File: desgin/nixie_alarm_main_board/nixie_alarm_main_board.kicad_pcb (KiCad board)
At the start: 2 copper layers, 79 parts, among them IC1 LM3488MM, IC2 HV5530PG-G, IC4 HV5530PG-G, IC5 TPH5200FNH, IC6 CD40109BQNSRQ1, IC7 AP7363-33D-13, IC8 MCP4018T-502E_LT, J1 DCPLUG 2x6.4mm 2A, J2 JST XH 2.54 3 pin, J3 USB_C_Receptacle_USB2.0_16P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

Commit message: filter caps
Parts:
- removed BZ1: Buzzer, Buzzer_Beeper:MagneticBuzzer_PUI_AT-0927-TT-6-R
- added C4: 100nF 25V, SamacSys_Parts:GRM033D70J224ME01D, F.Cu at (145.8, 94.5)
- added LS1: CEM-1203_42_, SamacSys_Parts:CEM-1203_42_, F.Cu at (135.7, 171.7)
- added Q1: SSM3K35AMFV,L3F, SamacSys_Parts:SSM3K35AMFVL3F, F.Cu at (132.2, 99.9)
- added R35: 10k, SamacSys_Parts:ERJUP6, F.Cu at (133.1, 95.4)
- added R7: 10k, SamacSys_Parts:ERJUP6, F.Cu at (141.2, 95.4)
- added R8: 1k, SamacSys_Parts:ERJUP6, F.Cu at (141.2, 99.7)
- R3, R4: value 5.1k -> 5.1kΩ; footprint SamacSys_Parts:ERJUP6 -> SamacSys_Parts:RESC2012X60N
- moved U1 124.7 mm to (69.2, 141.9)
- moved IC4 100.1 mm to (185.7, 61.5)
- moved R10 98.7 mm to (258.9, 135.2)
- moved R11 98.7 mm to (258.9, 137.3)
- moved R14 98.7 mm to (260.3, 121.9)
- moved R15 98.7 mm to (258.9, 143.8)
- moved R16 98.7 mm to (258.9, 145.9)
- moved R9 98.7 mm to (258.9, 133.0)
- moved C17 98.7 mm to (259.3, 166.5)
- moved C18 98.7 mm to (259.3, 169.3)
- moved J3 98.7 mm to (206.4, 176.5)
- moved R12 98.7 mm to (258.9, 139.5)
- moved R13 98.7 mm to (258.9, 141.6)
- moved C1 98.7 mm to (240.7, 168.2)
- moved C10 98.7 mm to (262.1, 133.2)
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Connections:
- L2 pad 1: Net-(IC1-ISEN) -> +12V
- U1 pad 24: DEBUG_UART_TX -> unconnected-(U1-IO47-Pad24)
- U1 pad 25: DEBUG_UART_RX -> unconnected-(U1-IO48-Pad25)
- U1 pad 36: unconnected-(U1-RXD0-Pad36) -> DEBUG_UART_RX
- U1 pad 37: unconnected-(U1-TXD0-Pad37) -> DEBUG_UART_TX
- U1 pad 38: BUZZER -> LED_DATA
- U1 pad 6: LED_DATA -> BUZZER

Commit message: new hv conv desgin
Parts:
- removed C2: 180uF 250V, Capacitor_THT:CP_Radial_D10.0mm_P7.50mm
- removed D1: STTH1003SBY-TR, SamacSys_Parts:STTH1003SBYTR
- removed IC5: TPH5200FNH, footprints:SOP Advance_TOS-L
- removed R9: 51.1kΩ, SamacSys_Parts:RESC1005X40N
- added C23: 100nF 25V, Capacitor_SMD:C_0805_2012Metric_Pad1.18x1.45mm_HandSolder, B.Cu at (261.2, 96.8)
- added C24: 100nF 25V, Capacitor_SMD:C_0805_2012Metric_Pad1.18x1.45mm_HandSolder, B.Cu at (272.8, 103.5)
- added C25: 100nF 25V, Capacitor_SMD:C_0805_2012Metric_Pad1.18x1.45mm_HandSolder, B.Cu at (261.2, 101.8)
- added C26: 4.7uF 450V, SamacSys_Parts:ECWFE2W475K, F.Cu at (226.6, 65.0)
- added C5: 100nF 25V, Capacitor_SMD:C_0805_2012Metric_Pad1.18x1.45mm_HandSolder, B.Cu at (215.1, 71.8)
- added C6: 100nF 25V, Capacitor_SMD:C_0805_2012Metric_Pad1.18x1.45mm_HandSolder, B.Cu at (268.0, 83.8)
- added C7: 100nF 25V, Capacitor_SMD:C_0805_2012Metric_Pad1.18x1.45mm_HandSolder, B.Cu at (268.0, 86.9)
- added C8: 100nF 25V, Capacitor_SMD:C_0805_2012Metric_Pad1.18x1.45mm_HandSolder, B.Cu at (268.0, 89.9)
- added C9: 100nF 25V, Capacitor_SMD:C_0805_2012Metric_Pad1.18x1.45mm_HandSolder, B.Cu at (268.0, 92.9)
- added D2: ES1G, SamacSys_Parts:DIOM5227X260N, F.Cu at (146.1, 162.6)
- added Q8: STL2N80K5, SamacSys_Parts:STL2N80K5, F.Cu at (146.2, 155.6)
- added R36: 51kΩ, Resistor_SMD:R_0805_2012Metric_Pad1.20x1.40mm_HandSolder, B.Cu at (272.8, 83.8)
- added R37: 51kΩ, Resistor_SMD:R_0805_2012Metric_Pad1.20x1.40mm_HandSolder, B.Cu at (272.8, 86.8)
- added R38: 51kΩ, Resistor_SMD:R_0805_2012Metric_Pad1.20x1.40mm_HandSolder, B.Cu at (272.8, 89.7)
- added R39: 51kΩ, Resistor_SMD:R_0805_2012Metric_Pad1.20x1.40mm_HandSolder, B.Cu at (272.8, 92.7)
- added R40: 51kΩ, Resistor_SMD:R_0805_2012Metric_Pad1.20x1.40mm_HandSolder, B.Cu at (272.8, 95.6)
- added R41: 51kΩ, Resistor_SMD:R_0805_2012Metric_Pad1.20x1.40mm_HandSolder, B.Cu at (272.8, 98.6)
- added R42: 5.1kΩ, Resistor_SMD:R_0805_2012Metric_Pad1.20x1.40mm_HandSolder, B.Cu at (261.2, 83.8)
- added R43: 5.1kΩ, Resistor_SMD:R_0805_2012Metric_Pad1.20x1.40mm_HandSolder, B.Cu at (261.2, 86.8)
- added R44: 27kΩ, Resistor_SMD:R_0805_2012Metric_Pad1.20x1.40mm_HandSolder, F.Cu at (131.3, 127.0)
- C1, C20, C21, IC1, IC6, IC7, IC8, J2, L1, LS1, PS1, Q1, Q2, Q3, Q4, Q5, Q6, Q7, R13, U1: moved to B.Cu
- C10, C14, C15, C16, C19, C22, C3, C4: footprint SamacSys_Parts:GRM033D70J224ME01D -> Capacitor_SMD:C_0805_2012Metric_Pad1.18x1.45mm_HandSolder; moved to B.Cu
- C11: value 12pF 50V -> 12pF 16V; moved to B.Cu
- C12: value 220pF 16V -> 220pF 50V; footprint SamacSys_Parts:GRM033D70J224ME01D -> Capacitor_SMD:C_0805_2012Metric_Pad1.18x1.45mm_HandSolder; moved to B.Cu
- C13: value 10pF 50V -> 10pF 25V; footprint SamacSys_Parts:GRM033D70J224ME01D -> Capacitor_SMD:C_0805_2012Metric_Pad1.18x1.45mm_HandSolder; moved to B.Cu
- C17, C18: footprint SamacSys_Parts:CAPC2012X135N -> Capacitor_SMD:C_0805_2012Metric_Pad1.18x1.45mm_HandSolder; moved to B.Cu
- L2: value 330uH 6A -> 180uH 0.9A 6.3mΩ; footprint SamacSys_Parts:INDPM250280X2050N -> Inductor_SMD:L_12x12mm_H6mm; moved to B.Cu
- R1, R14, R17, R18, R19, R2, R20, R24, R26, R29, R30, R32, R34, R35, R5, R6, R7, R8: footprint SamacSys_Parts:ERJUP6 -> Resistor_SMD:R_0805_2012Metric_Pad1.20x1.40mm_HandSolder; moved to B.Cu
- R10, R12, R15: footprint SamacSys_Parts:RESC1005X40N -> Resistor_SMD:R_1206_3216Metric_Pad1.30x1.75mm_HandSolder; moved to B.Cu
- R11: footprint SamacSys_Parts:RESC1005X40N -> Resistor_SMD:R_0805_2012Metric_Pad1.20x1.40mm_HandSolder; moved to B.Cu
- R16: value 14.7kΩ -> 14.3kΩ; footprint SamacSys_Parts:RESC1005X40N -> Resistor_SMD:R_0805_2012Metric_Pad1.20x1.40mm_HandSolder; moved to B.Cu
- R21, R27: value 402kΩ 1/4W -> 390kΩ 1/2W; footprint SamacSys_Parts:RESC2012X60N -> Resistor_SMD:R_0805_2012Metric_Pad1.20x1.40mm_HandSolder; moved to B.Cu
- R22, R23, R25, R28, R31, R33: value 25kΩ -> 27kΩ; footprint SamacSys_Parts:RESC2012X60N -> Resistor_SMD:R_0805_2012Metric_Pad1.20x1.40mm_HandSolder; moved to B.Cu
- R3, R4: footprint SamacSys_Parts:RESC2012X60N -> Resistor_SMD:R_0805_2012Metric_Pad1.20x1.40mm_HandSolder; moved to B.Cu
- moved C10 223.0 mm to (39.0, 133.9), turned to 180 degrees
- moved C12 223.0 mm to (39.0, 136.3), turned to 180 degrees
- moved C13 223.0 mm to (39.0, 138.7), turned to 180 degrees
- moved C16 223.0 mm to (39.0, 141.1), turned to 180 degrees
- moved R14 214.8 mm to (45.5, 121.9), turned to 180 degrees
- moved C11 214.2 mm to (45.7, 126.2), turned to 180 degrees
- moved C17 212.9 mm to (46.4, 166.5), turned to 180 degrees
- moved C18 212.9 mm to (46.4, 169.3), turned to 180 degrees
- moved C19 212.0 mm to (46.9, 171.8), turned to 180 degrees
- moved IC8 207.1 mm to (52.3, 130.4), turned to 180 degrees
- moved R10 206.0 mm to (52.9, 135.4), turned to 180 degrees
- moved R11 206.0 mm to (52.9, 137.6), turned to 180 degrees
- moved R12 206.0 mm to (52.9, 139.7), turned to 180 degrees
- moved R13 206.0 mm to (52.9, 141.9), turned to 180 degrees
- moved R15 206.0 mm to (52.9, 144.0), turned to 180 degrees
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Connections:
- IC6 pad 1: +5V -> +3.3V
- IC6 pad 15: +5V -> +3.3V
- IC6 pad 2: +5V -> +3.3V
- Q2 pad 2: GND -> Net-(Q2-S)
- Q3 pad 2: GND -> Net-(Q3-S)
- Q4 pad 2: GND -> Net-(Q4-S)
- Q5 pad 2: GND -> Net-(Q5-S)
- Q6 pad 2: GND -> Net-(Q6-S)
- Q7 pad 2: GND -> Net-(Q7-S)
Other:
- board outline added: 157.3 x 59 mm
- board text added: "FRONT"

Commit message: traces for nixie tubes
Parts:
- removed NE3, NE4: 90V 0.3mA, nixie:neon_lamp
- removed PS1: TPS566242DRLR, SamacSys_Parts:SOT50P160X60-6N
- removed Q8: STL2N80K5, SamacSys_Parts:STL2N80K5
- removed R6: 15kΩ, Resistor_SMD:R_0805_2012Metric_Pad1.20x1.40mm_HandSolder
- added C2: 12uF 250V, Capacitor_THT:CP_Radial_D10.0mm_P5.00mm, F.Cu at (204.0, 69.2)
- added C27: 10pF 25V, Capacitor_SMD:C_0805_2012Metric_Pad1.18x1.45mm_HandSolder, B.Cu at (123.6, 93.8)
- added IC3: TPS563219ADDFR, SamacSys_Parts:SOT65P280X110-8N, B.Cu at (62.4, 151.2)
- added NE1: 90V 0.3mA, nixie:neon_lamp, F.Cu at (124.4, 42.0)
- added NE2: 90V 0.3mA, nixie:neon_lamp, F.Cu at (173.1, 42.0)
- added Q9: TPH5200FNH,L1Q, Package_SO:SO-8_3.9x4.9mm_P1.27mm, B.Cu at (211.5, 109.5)
- C26: value 4.7uF 450V -> 100nF 25V; footprint SamacSys_Parts:ECWFE2W475K -> Capacitor_SMD:C_0805_2012Metric_Pad1.18x1.45mm_HandSolder; moved to B.Cu
- D2, J1, J3, R44: moved to B.Cu
- IC6, L2, Q2, Q3, Q4, Q5, Q6, Q7: moved to F.Cu
- L1: value XAL5030-222MEC -> 2.2uH 9.2A
- R1: value 220kΩ -> 56kΩ
- R2: value 30kΩ -> 10kΩ
- moved C23 194.0 mm to (67.3, 104.3)
- moved C24 194.0 mm to (78.9, 111.1)
- moved C25 194.0 mm to (67.3, 109.3)
- moved C6 194.0 mm to (74.1, 91.4)
- moved C7 194.0 mm to (74.1, 94.4)
- moved C8 194.0 mm to (74.1, 97.4)
- moved C9 194.0 mm to (74.1, 100.4)
- moved R36 194.0 mm to (78.9, 91.3)
- moved R37 194.0 mm to (78.9, 94.3)
- moved R38 194.0 mm to (78.9, 97.2)
- moved R39 194.0 mm to (78.9, 100.2)
- moved R40 194.0 mm to (78.9, 103.2)
- moved R41 194.0 mm to (78.9, 106.1)
- moved R42 194.0 mm to (67.4, 91.3)
- moved R43 194.0 mm to (67.4, 94.3)
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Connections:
- C26 pad 1: HV -> Net-(IC3-SW)
- C26 pad 2: GND -> Net-(IC3-VBST)
- IC2 pad 1: N2_0 -> N2_1
- IC2 pad 10: N2_9 -> N2_0
- IC2 pad 11: N1_0 -> NEON_1
- IC2 pad 12: N1_1 -> N3_1
- IC2 pad 13: N1_2 -> N3_2
- IC2 pad 14: N1_3 -> N3_3
- IC2 pad 15: N1_4 -> N3_4
- IC2 pad 16: N1_5 -> N3_5
- IC2 pad 17: N1_6 -> N3_6
- IC2 pad 18: N1_7 -> N3_7
- IC2 pad 19: N1_8 -> N3_8
- IC2 pad 2: N2_1 -> N2_2
- IC2 pad 20: N1_9 -> N3_9
- IC2 pad 21: NEON_1 -> N3_0
- IC2 pad 22: NEON_2 -> unconnected-(IC2-HVOUT32-Pad22)
- IC2 pad 3: N2_2 -> N2_3
- IC2 pad 35: N3_0 -> N1_1
- IC2 pad 36: N3_1 -> N1_2
- IC2 pad 37: N3_2 -> N1_3
- IC2 pad 38: N3_3 -> N1_4
- IC2 pad 39: N3_4 -> N1_5
- IC2 pad 4: N2_3 -> N2_4
- IC2 pad 40: N3_5 -> N1_6
- IC2 pad 41: N3_6 -> N1_7
- IC2 pad 42: N3_7 -> N1_8
- IC2 pad 43: N3_8 -> N1_9
- IC2 pad 44: N3_9 -> N1_0
- IC2 pad 5: N2_4 -> N2_5
- IC2 pad 6: N2_5 -> N2_6
- IC2 pad 7: N2_6 -> N2_7
- IC2 pad 8: N2_7 -> N2_8
- IC2 pad 9: N2_8 -> N2_9
- IC4 pad 1: N5_0 -> NEON_2
- IC4 pad 11: N4_0 -> N5_0
- IC4 pad 12: N4_1 -> unconnected-(IC4-HVOUT22-Pad12)
- IC4 pad 13: N4_2 -> N6_1
- IC4 pad 14: N4_3 -> N6_2
- IC4 pad 15: N4_4 -> N6_3
- IC4 pad 16: N4_5 -> N6_4
- IC4 pad 17: N4_6 -> N6_5
- IC4 pad 18: N4_7 -> N6_6
- IC4 pad 19: N4_8 -> N6_7
- IC4 pad 20: N4_9 -> N6_8
- IC4 pad 21: unconnected-(IC4-HVOUT31-Pad21) -> N6_9
- IC4 pad 22: unconnected-(IC4-HVOUT32-Pad22) -> N6_0
- IC4 pad 35: N6_0 -> N4_1
- IC4 pad 36: N6_1 -> N4_2
- IC4 pad 37: N6_2 -> N4_3
- IC4 pad 38: N6_3 -> N4_4
- IC4 pad 39: N6_4 -> N4_5
- IC4 pad 40: N6_5 -> N4_6
- IC4 pad 41: N6_6 -> N4_7
- IC4 pad 42: N6_7 -> N4_8
- IC4 pad 43: N6_8 -> N4_9
- IC4 pad 44: N6_9 -> N4_0
- L1 pad 1: Net-(PS1-SW) -> Net-(IC3-SW)
- N2 pad 0: unconnected-(N2-Pad0) -> N2_0
- N2 pad 1: unconnected-(N2-Pad1) -> N2_1
- N2 pad 2: unconnected-(N2-Pad2) -> N2_2
- N2 pad 3: unconnected-(N2-Pad3) -> N2_3
- N2 pad 4: unconnected-(N2-Pad4) -> N2_4
- N2 pad 5: unconnected-(N2-Pad5) -> N2_5
- N2 pad 6: unconnected-(N2-Pad6) -> N2_6
- N2 pad 7: unconnected-(N2-Pad7) -> N2_7
- N2 pad 8: unconnected-(N2-Pad8) -> N2_8
- N2 pad 9: unconnected-(N2-Pad9) -> N2_9
- R5 pad 1: +12V -> Net-(IC3-PG)
- R5 pad 2: Net-(PS1-EN) -> +5V
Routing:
- net Net-(IC2-~{BL}): track 0.00 -> 115.1 mm, vias 0 -> 3
- net Net-(IC2-~{LE}): track 0.00 -> 112.9 mm, vias 0 -> 3
- net Net-(IC2-CLK): track 0.00 -> 111.2 mm, vias 0 -> 3
- net HV: track 0.00 -> 109.5 mm
- net N4_1: track 0.00 -> 56.5 mm
- net N3_0: track 0.00 -> 53.5 mm
- net Net-(IC4-DATA_INPUT): track 0.00 -> 53.0 mm, vias 0 -> 2
- net N4_2: track 0.00 -> 52.7 mm
- net N3_9: track 0.00 -> 49.8 mm
- net N4_3: track 0.00 -> 48.6 mm
- net N3_1: track 0.00 -> 45.3 mm
- net N3_8: track 0.00 -> 43.8 mm
- net N3_2: track 0.00 -> 43.5 mm
- net N4_0: track 0.00 -> 43.3 mm
- net N4_4: track 0.00 -> 42.5 mm
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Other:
- board size 157.3 x 59 mm -> 144.3 x 64.5 mm
- board text added: "${REFERENCE}"

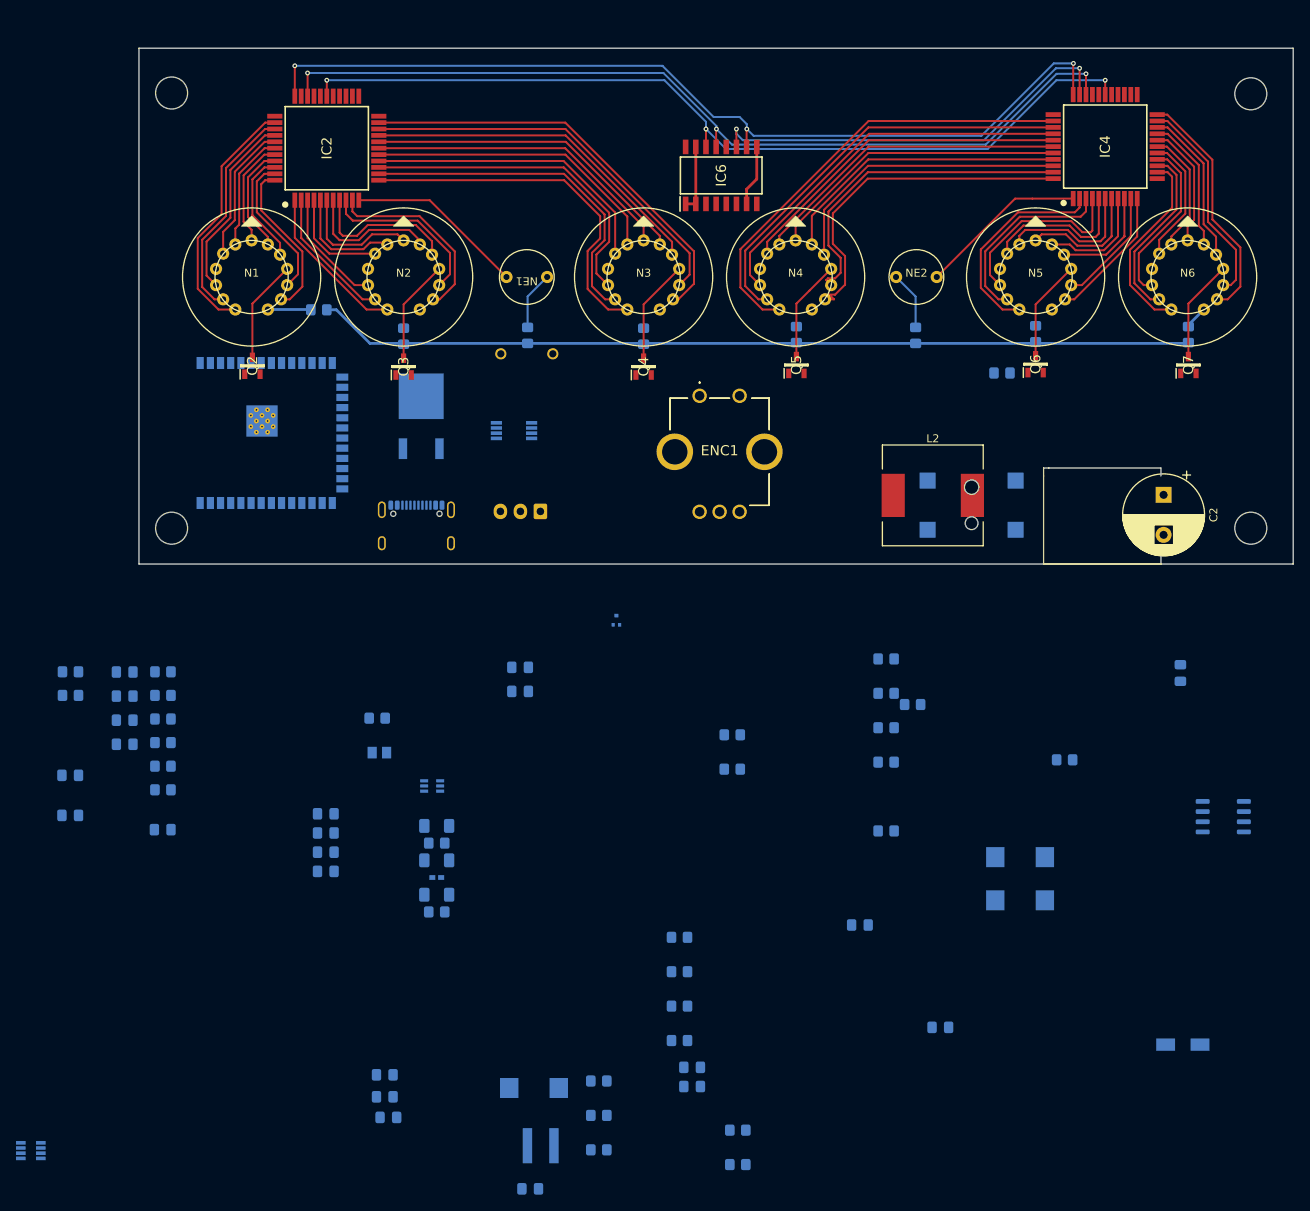
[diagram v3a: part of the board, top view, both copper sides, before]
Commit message: all components in board footprint
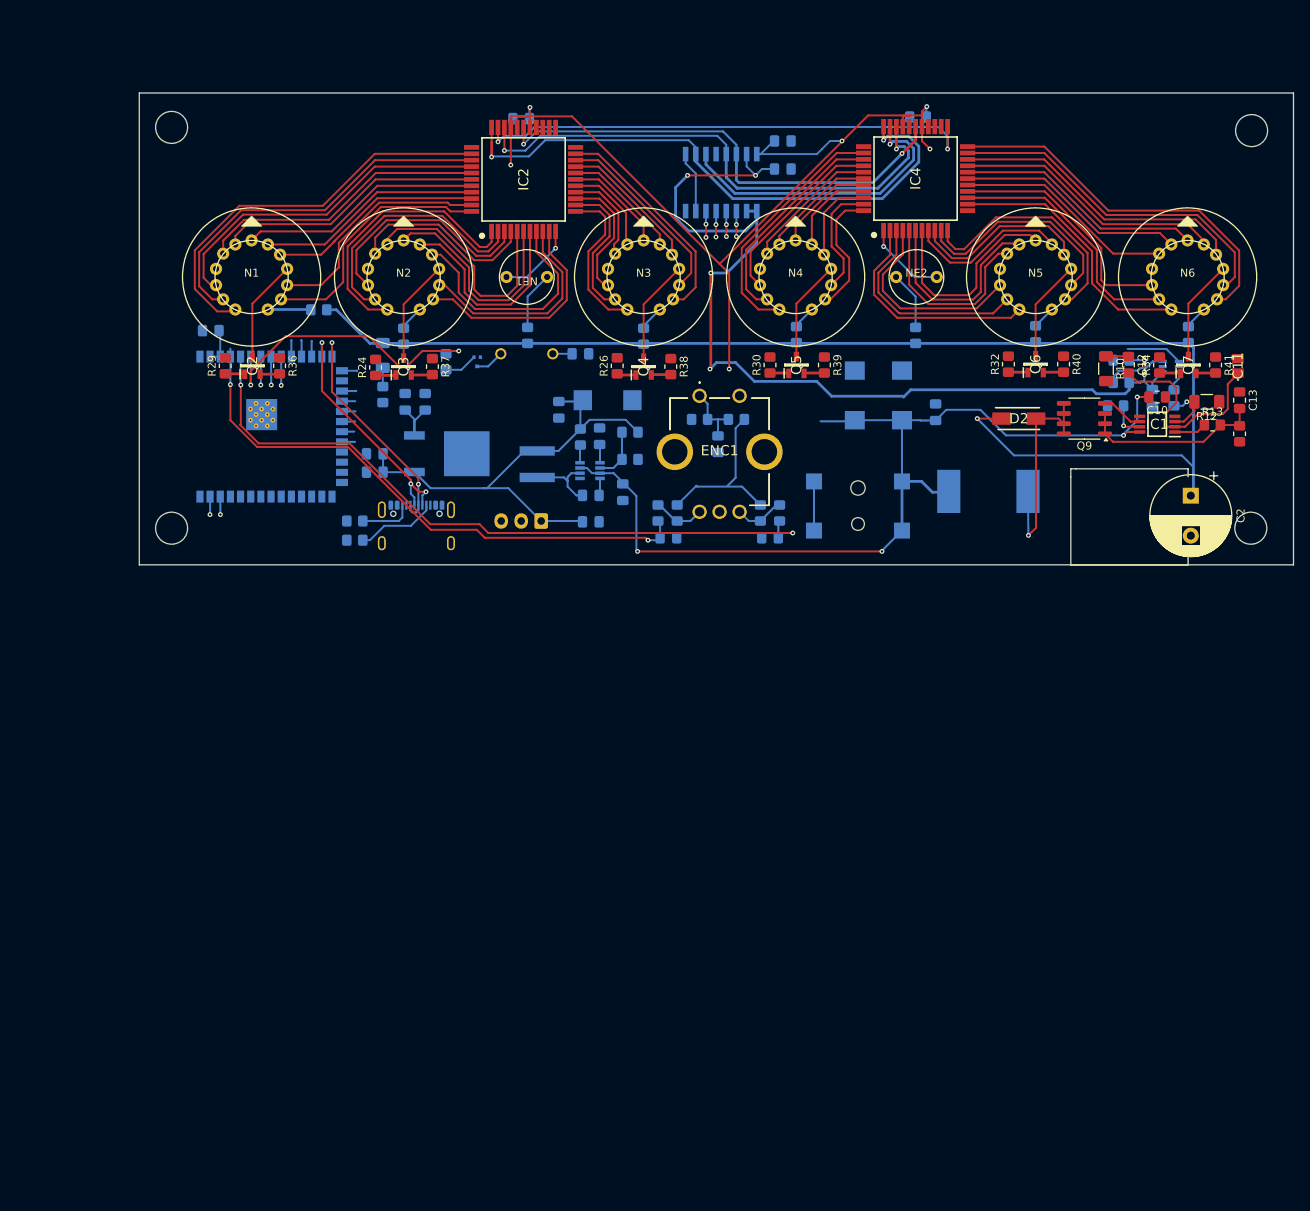
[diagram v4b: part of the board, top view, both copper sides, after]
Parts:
- added C28: 100nF 25V, Capacitor_SMD:C_0805_2012Metric_Pad1.18x1.45mm_HandSolder, B.Cu at (84.9, 48.7)
- C10, C11, C12, C13, D2, IC1, Q9, R10, R12, R14, R24, R26, R29, R30, R32, R34, R36, R37, R38, R39, R40, R41: moved to F.Cu
- IC6, L2: moved to B.Cu
- R13: footprint SamacSys_Parts:RESC1005X40N -> Resistor_SMD:R_0805_2012Metric_Pad1.20x1.40mm_HandSolder; moved to F.Cu
- moved R41 141.9 mm to (210.5, 53.0), turned to -90 degrees
- moved R43 137.9 mm to (198.7, 52.4), turned to 0 degrees
- moved R42 136.2 mm to (198.7, 55.2), turned to 0 degrees
- moved C13 127.4 mm to (213.5, 57.4), turned to -90 degrees
- moved C8 124.6 mm to (173.3, 22.0)
- moved R40 123.3 mm to (191.5, 52.9), turned to -90 degrees
- moved C16 119.1 mm to (202.6, 57.1), turned to -90 degrees
- moved C11 117.7 mm to (213.3, 53.1), turned to 90 degrees
- moved C10 116.3 mm to (203.2, 57.0)
- moved C12 116.2 mm to (199.6, 53.0), turned to -90 degrees
- moved R14 113.5 mm to (213.5, 61.6), turned to -90 degrees
- moved R13 112.3 mm to (210.1, 60.5), turned to 0 degrees
- moved R12 112.0 mm to (209.4, 57.6)
- moved IC3 110.1 mm to (132.3, 66.2), turned to 0 degrees
- moved R11 107.7 mm to (205.3, 57.1), turned to 90 degrees
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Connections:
- ENC1 pad 1: (no net) -> Net-(C4-Pad1)
- ENC1 pad 2: (no net) -> GND
- ENC1 pad A1: (no net) -> Net-(ENC1-PadA1)
- ENC1 pad B1: (no net) -> Net-(ENC1-PadB1)
- ENC1 pad C1: (no net) -> GND
- R17 pad 1: Net-(ENC1-PadA) -> Net-(ENC1-PadA1)
- R18 pad 2: Net-(ENC1-PadB) -> Net-(ENC1-PadB1)
- R19 pad 1: Net-(ENC1-PadB) -> Net-(ENC1-PadB1)
- R20 pad 1: Net-(ENC1-PadA) -> Net-(ENC1-PadA1)
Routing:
- net +12V: track 0.00 -> 243.9 mm, vias 0 -> 10
- net +3.3V: track 8.39 -> 137.6 mm, vias 0 -> 6
- net ENC_B: track 0.00 -> 87.8 mm, vias 0 -> 2
- net +5V: track 0.00 -> 81.7 mm
- net ENC_A: track 0.00 -> 70.9 mm, vias 0 -> 2
- net Net-(IC2-DATA_INPUT): track 0.00 -> 63.7 mm, vias 0 -> 2
- net HV: track 109.5 -> 165.3 mm, vias 0 -> 1
- net Net-(IC2-CLK): track 111.2 -> 60.9 mm, vias 3 -> 2
- net Net-(IC2-~{LE}): track 112.9 -> 66.5 mm, vias 3 -> 2
- net Net-(IC2-~{BL}): track 115.1 -> 74.6 mm, vias 3 -> 2
- net BUZZER: track 0.00 -> 37.5 mm, vias 0 -> 2
- net USB_D-: track 0.00 -> 31.2 mm, vias 0 -> 3
- net USB_D+: track 0.00 -> 29.1 mm, vias 0 -> 2
- net Net-(D2-A): track 0.00 -> 28.2 mm, vias 0 -> 1
- net N4_0: track 43.3 -> 16.2 mm
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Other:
- board size 144.3 x 64.5 mm -> 144.3 x 59 mm
